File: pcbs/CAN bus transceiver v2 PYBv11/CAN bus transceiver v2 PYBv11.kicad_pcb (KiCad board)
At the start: 2 copper layers, 5 parts, among them P1 CONN_01X16, P2 CONN_01X02, P3 CONN_01X16, U1 TCAN337GDR, U2 TCAN337GDR

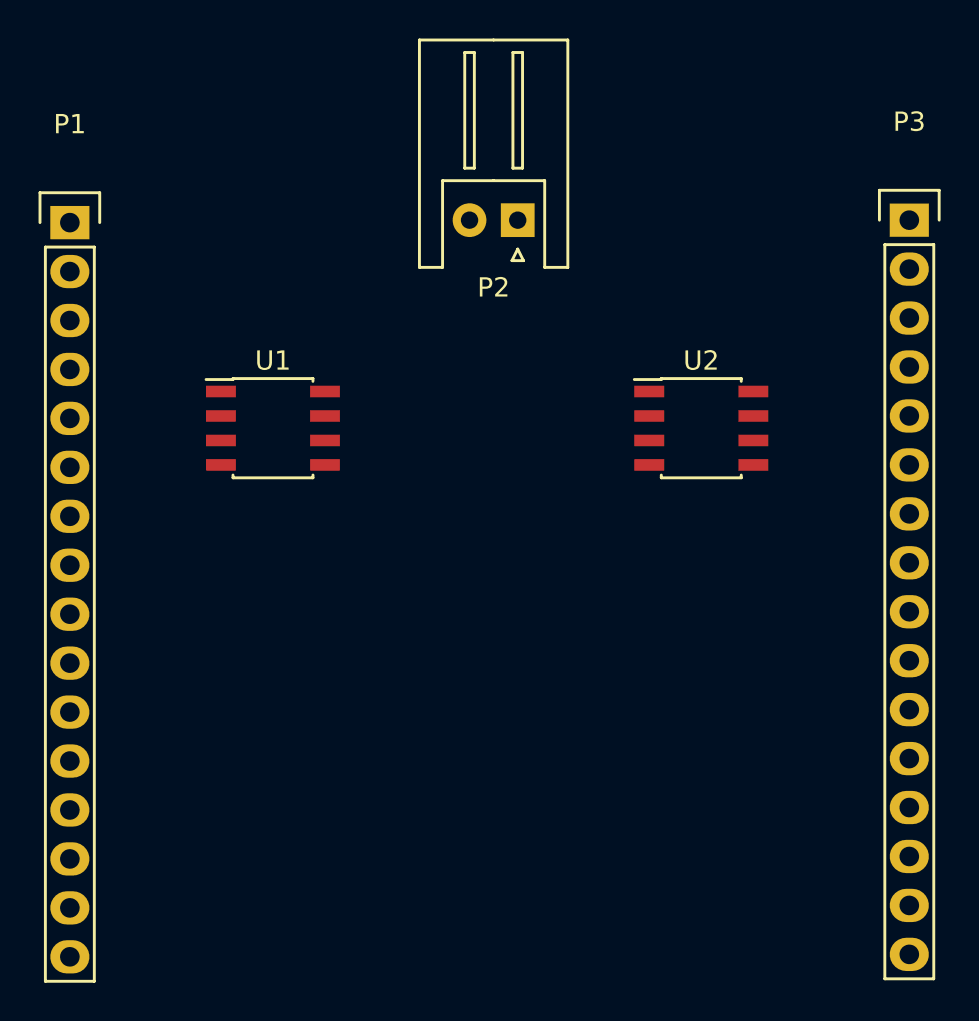
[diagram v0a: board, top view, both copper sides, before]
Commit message: working on CAN bus transceiver v2 PYBv11 shield
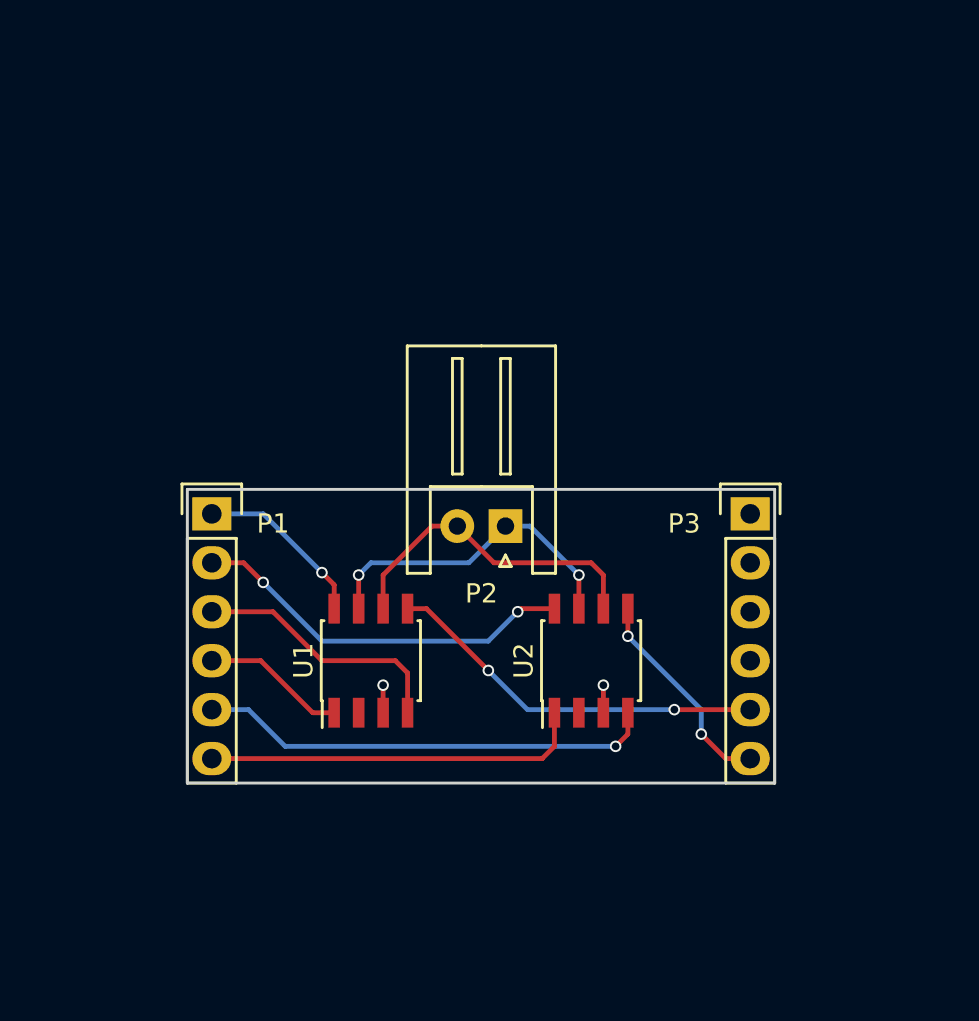
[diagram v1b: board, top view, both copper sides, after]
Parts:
- P1, P3: value CONN_01X16 -> CONN_01X06; footprint Pin_Headers:Pin_Header_Straight_1x16 -> Pin_Headers:Pin_Header_Straight_1x06
- moved P3 17.3 mm to (111.1, 91.4)
- moved P1 16.8 mm to (83.2, 91.4)
- moved P2 15.9 mm to (98.4, 92.1)
- moved U2 13.4 mm to (102.9, 99.1), turned to 90 degrees
- moved U1 13.1 mm to (91.4, 99.1), turned to 90 degrees
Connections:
- P3 pad 1: Net-(P3-Pad1) -> (no net)
- P3 pad 4: Net-(P3-Pad4) -> (no net)
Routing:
- net Net-(P1-Pad5): track 0.00 -> 23.8 mm, vias 0 -> 1
- net Net-(P1-Pad2): track 0.00 -> 20.2 mm, vias 0 -> 2
- net Net-(P3-Pad5): track 0.00 -> 20.0 mm, vias 0 -> 2
- net Net-(P1-Pad6): track 0.00 -> 19.8 mm
- net Net-(P2-Pad2): track 0.00 -> 17.0 mm
- net Net-(P2-Pad1): track 0.00 -> 17.0 mm, vias 0 -> 2
- net Net-(P1-Pad3): track 0.00 -> 13.5 mm
- net Net-(P3-Pad6): track 0.00 -> 11.2 mm, vias 0 -> 2
- net Net-(P1-Pad1): track 0.00 -> 9.11 mm, vias 0 -> 1
- net Net-(P1-Pad4): track 0.00 -> 7.47 mm
- net +3V3: track 0.00 -> 2.86 mm, vias 0 -> 2
- added copper zone on B.Cu, net +3V3
- added copper zone on F.Cu, net GND
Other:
- board outline added: 30.5 x 15.2 mm
- board text added: "3V3"
- board text added: "GND"
- board text added: "Y1"
- board text added: "Y11"
- board text added: "Y12"
- board text added: "Y2"
- board text added: "Y3"
- board text added: "Y4"
- board text added: "Y5"
- board text added: "Y6"

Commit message: working on CAN bus transceiver v2 PYBv11 shield
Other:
- board text added: "CAN bus transceiver shield v2 for PyBoard v 1.1"
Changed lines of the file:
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@@
     (links 16)
     (no_connects 0)
-    (area 81.839999 90.094999 112.470001 105.485001)
+    (area 63.270001 74.77 116.158334 117.000001)
     (thickness 1.6)
-    (drawings 18)
+    (drawings 19)
     (tracks 65)
     (zones 0)
@@
     (visible_elements FFFFFF7F)
     (pcbplotparams
-      (layerselection 0x00030_80000001)
-      (usegerberextensions false)
+      (layerselection 0x010f0_80000001)
+      (usegerberextensions true)
+      (gerberprecision 5)
       (excludeedgelayer true)
       (linewidth 0.100000)
@@
       (outputformat 1)
       (mirror false)
-      (drillshape 1)
+      (drillshape 0)
       (scaleselection 1)
-      (outputdirectory ""))
+      (outputdirectory plots/))
   )
   (net 0 "")
@@
     )
   )
+  (gr_text "CAN bus transceiver shield v2 for PyBoard v 1.1" (at 97.028 104.648) (layer B.SilkS)
+    (effects (font (size 0.5 0.5) (thickness 0.1)) (justify mirror))
+  )
   (gr_text 3V3 (at 108.712 93.98) (layer B.SilkS)

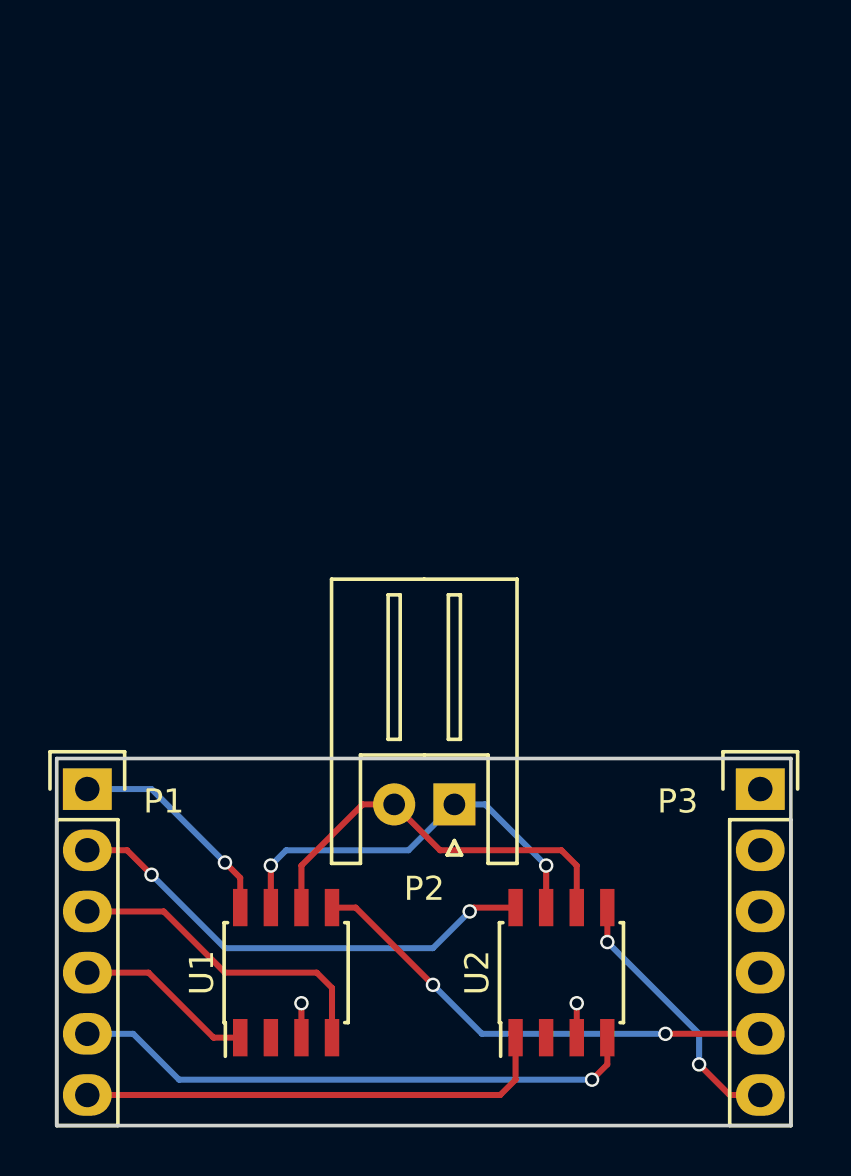
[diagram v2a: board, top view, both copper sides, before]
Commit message: working on CAN bus transceiver v2 PYBv11 shield
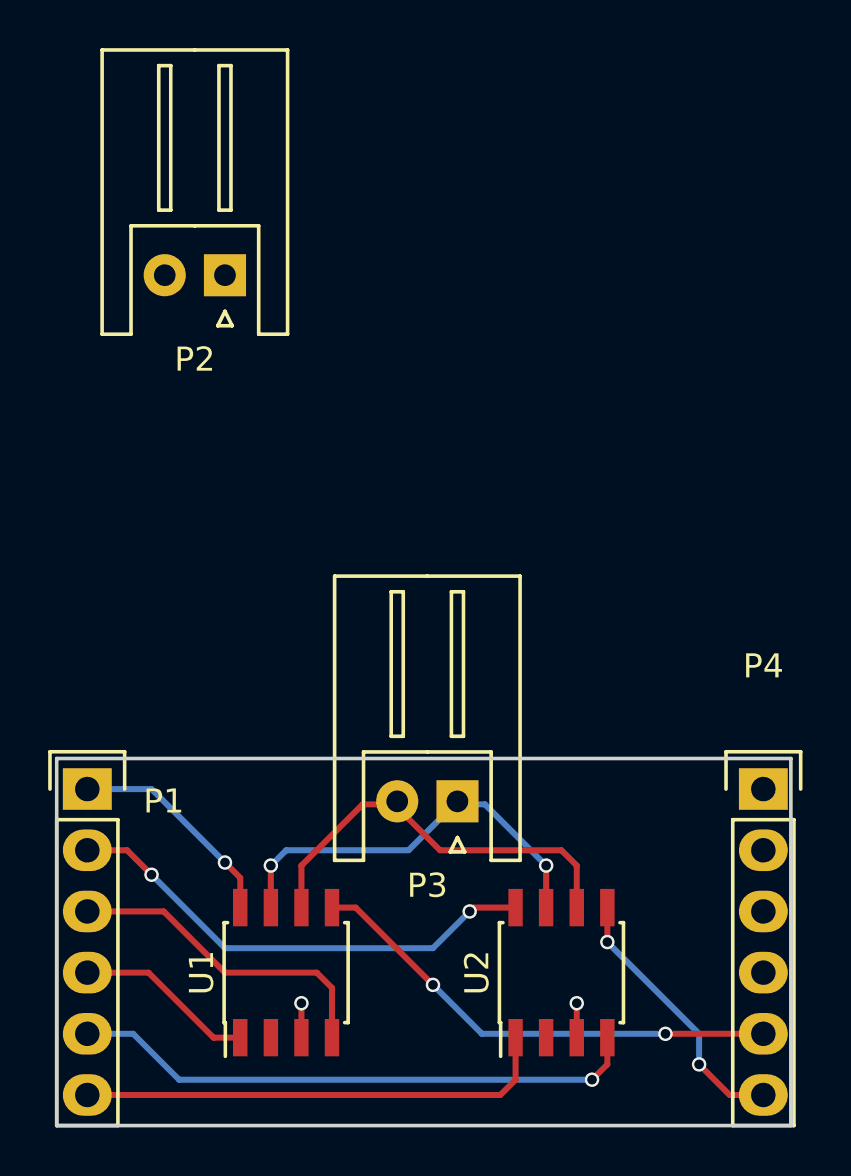
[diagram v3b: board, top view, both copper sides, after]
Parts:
- added P4: CONN_01X06, Pin_Headers:Pin_Header_Straight_1x06, F.Cu at (111.3, 91.4)
- P3: value CONN_01X06 -> CONN_01X02; footprint Pin_Headers:Pin_Header_Straight_1x06 -> Connectors_JST:JST_XH_S02B-XH-A_02x2.50mm_Angled
- moved P2 23.9 mm to (88.9, 70.1)
- moved P3 12.6 mm to (98.6, 91.9), turned to 180 degrees
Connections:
- P2 pad 1: Net-(P2-Pad1) -> (no net)
- P2 pad 2: Net-(P2-Pad2) -> (no net)
- P3 pad 1: (no net) -> Net-(P3-Pad1)
- P3 pad 2: +3V3 -> Net-(P3-Pad2)
- U1 pad 5: Net-(P3-Pad5) -> Net-(P4-Pad5)
- U1 pad 6: Net-(P2-Pad2) -> Net-(P3-Pad2)
- U1 pad 7: Net-(P2-Pad1) -> Net-(P3-Pad1)
- U2 pad 5: Net-(P3-Pad6) -> Net-(P4-Pad6)
- U2 pad 6: Net-(P2-Pad2) -> Net-(P3-Pad2)
- U2 pad 7: Net-(P2-Pad1) -> Net-(P3-Pad1)
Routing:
- net Net-(P4-Pad5): track 0.00 -> 20.0 mm, vias 0 -> 2
- net Net-(P3-Pad5): track 20.0 -> 0.00 mm, vias 2 -> 0
- net Net-(P3-Pad2): track 0.00 -> 17.0 mm
- net Net-(P2-Pad2): track 17.0 -> 0.00 mm
- net Net-(P3-Pad1): track 0.00 -> 17.0 mm, vias 0 -> 2
- net Net-(P2-Pad1): track 17.0 -> 0.00 mm, vias 2 -> 0
- net Net-(P4-Pad6): track 0.00 -> 11.2 mm, vias 0 -> 2
- net Net-(P3-Pad6): track 11.2 -> 0.00 mm, vias 2 -> 0

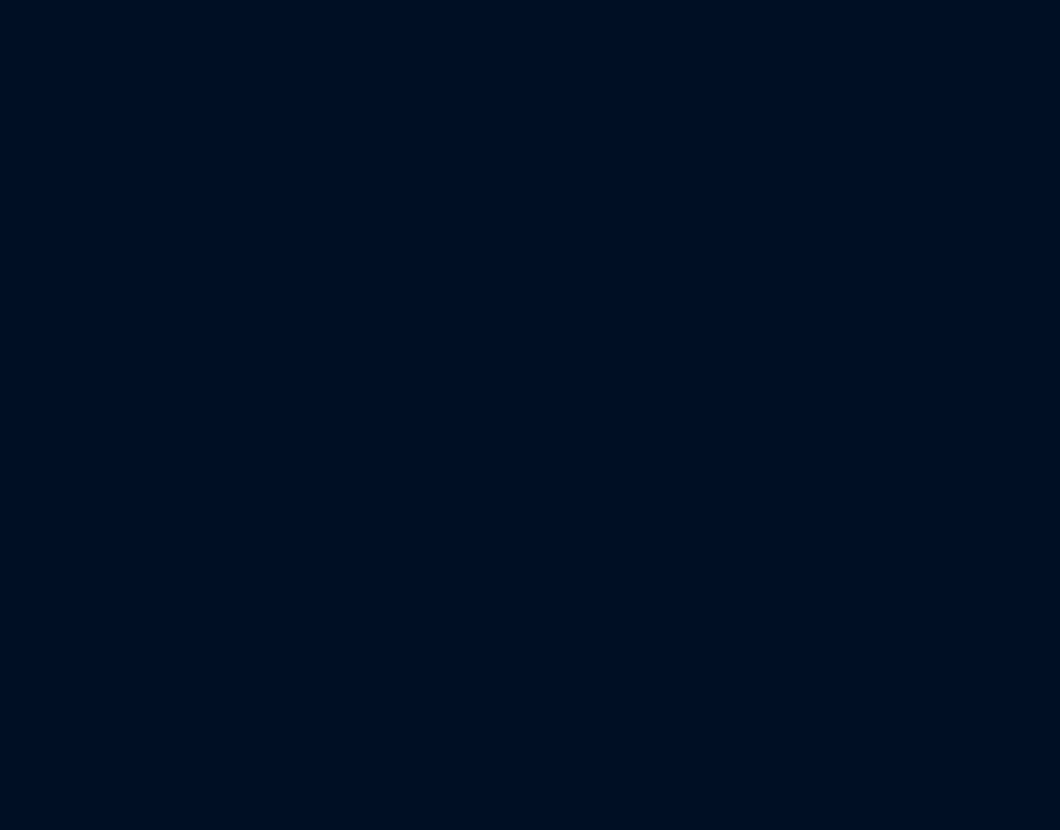
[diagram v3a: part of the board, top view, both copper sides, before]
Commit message: working on CAN bus transceiver v2 PYBv11 shield
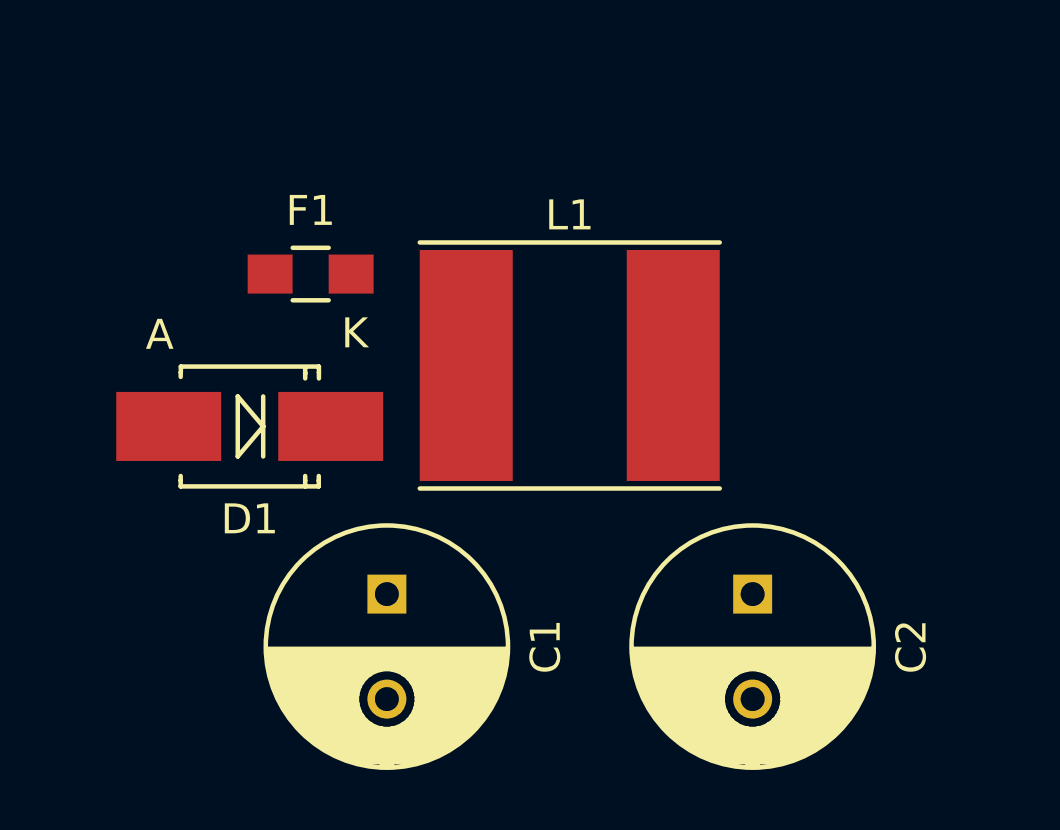
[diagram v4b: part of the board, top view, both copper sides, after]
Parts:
- added C1: CP1, Capacitors_ThroughHole:C_Radial_D8_L11.5_P3.5, F.Cu at (92.5, 135.6)
- added C2: CP1, Capacitors_ThroughHole:C_Radial_D8_L11.5_P3.5, F.Cu at (104.6, 135.6)
- added D1: ZENER, Diodes_SMD:SMB_Handsoldering, F.Cu at (87.9, 130.0)
- added F1: FUSE, Resistors_SMD:R_0805_HandSoldering, F.Cu at (89.9, 125.0)
- added L1: INDUCTOR, Inductors:Inductor_Taiyo-Yuden_NR-80xx_HandSoldering, F.Cu at (98.6, 128.0)

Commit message: doc: added docs for Pioneer AVH-X7500BT and Texas Instruments LM3489
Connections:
- C1 pad 2: Net-(C1-Pad2) -> GND
- C2 pad 2: Net-(C1-Pad2) -> GND
- D1 pad 2: Net-(C1-Pad2) -> GND
- F1 pad 1: (no net) -> +12V
- P2 pad 1: (no net) -> +12V
- P2 pad 2: (no net) -> GND
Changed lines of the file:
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@@
 (kicad_pcb (version 4) (host pcbnew 4.0.4-stable)
   (general
-    (links 22)
-    (no_connects 6)
+    (links 25)
+    (no_connects 9)
     (area 81.839999 90.094999 112.470001 105.485001)
     (thickness 1.6)
@@
   (net 11 "Net-(P4-Pad5)")
   (net 12 "Net-(P4-Pad6)")
-  (net 13 "Net-(C1-Pad2)")
-  (net 14 "Net-(C1-Pad1)")
-  (net 15 "Net-(C2-Pad1)")
+  (net 13 "Net-(C1-Pad1)")
+  (net 14 "Net-(C2-Pad1)")
+  (net 15 +12V)
   (net_class Default "This is the default net class."
     (clearance 0.2)
@@
     (uvia_dia 0.3)
     (uvia_drill 0.1)
+    (add_net +12V)
     (add_net +3V3)
     (add_net GND)
     (add_net "Net-(C1-Pad1)")
-    (add_net "Net-(C1-Pad2)")
     (add_net "Net-(C2-Pad1)")
     (add_net "Net-(P1-Pad1)")
@@
     (fp_line (start -0.3 -2.1) (end 0.3 -2.1) (layer F.SilkS) (width 0.15))
     (fp_line (start 0.3 -2.1) (end 0 -1.5) (layer F.SilkS) (width 0.15))
-    (pad 1 thru_hole rect (at 0 0 180) (size 1.75 1.75) (drill 0.9) (layers *.Cu *.Mask F.SilkS))
-    (pad 2 thru_hole circle (at 2.5 0 180) (size 1.75 1.75) (drill 0.9) (layers *.Cu *.Mask F.SilkS))
+    (pad 1 thru_hole rect (at 0 0 180) (size 1.75 1.75) (drill 0.9) (layers *.Cu *.Mask F.SilkS)
+      (net 15 +12V))
+    (pad 2 thru_hole circle (at 2.5 0 180) (size 1.75 1.75) (drill 0.9) (layers *.Cu *.Mask F.SilkS)
+      (net 7 GND))
     (model Connectors_JST.3dshapes/JST_XH_S02B-XH-A_02x2.50mm_Angled.wrl
       (at (xyz 0 0 0))
@@
     (fp_circle (center 1.75 0) (end 1.75 -4.3) (layer F.CrtYd) (width 0.05))
     (pad 2 thru_hole circle (at 3.5 0 270) (size 1.3 1.3) (drill 0.8) (layers *.Cu *.Mask F.SilkS)
-      (net 13 "Net-(C1-Pad2)"))
+      (net 7 GND))
     (pad 1 thru_hole rect (at 0 0 270) (size 1.3 1.3) (drill 0.8) (layers *.Cu *.Mask F.SilkS)
-      (net 14 "Net-(C1-Pad1)"))
+      (net 13 "Net-(C1-Pad1)"))
     (model Capacitors_ThroughHole.3dshapes/C_Radial_D8_L11.5_P3.5.wrl
       (at (xyz 0 0 0))
@@
     (fp_circle (center 1.75 0) (end 1.75 -4.3) (layer F.CrtYd) (width 0.05))
     (pad 2 thru_hole circle (at 3.5 0 270) (size 1.3 1.3) (drill 0.8) (layers *.Cu *.Mask F.SilkS)
-      (net 13 "Net-(C1-Pad2)"))
+      (net 7 GND))
     (pad 1 thru_hole rect (at 0 0 270) (size 1.3 1.3) (drill 0.8) (layers *.Cu *.Mask F.SilkS)
-      (net 15 "Net-(C2-Pad1)"))
+      (net 14 "Net-(C2-Pad1)"))
     (model Capacitors_ThroughHole.3dshapes/C_Radial_D8_L11.5_P3.5.wrl
       (at (xyz 0 0 0))
@@
     (fp_line (start 2.30124 -1.99898) (end 2.30124 -1.80086) (layer F.SilkS) (width 0.15))
     (pad 1 smd rect (at -2.70002 0 180) (size 3.50012 2.30124) (layers F.Cu F.Paste F.Mask)
-      (net 14 "Net-(C1-Pad1)"))
+      (net 13 "Net-(C1-Pad1)"))
     (pad 2 smd rect (at 2.70002 0 180) (size 3.50012 2.30124) (layers F.Cu F.Paste F.Mask)
-      (net 13 "Net-(C1-Pad2)"))
+      (net 7 GND))
     (model Diodes_SMD.3dshapes/SMB_Handsoldering.wrl
       (at (xyz 0 0 0))
@@
     (fp_line (start 0.6 0.875) (end -0.6 0.875) (layer F.SilkS) (width 0.15))
     (fp_line (start -0.6 -0.875) (end 0.6 -0.875) (layer F.SilkS) (width 0.15))
-    (pad 1 smd rect (at -1.35 0) (size 1.5 1.3) (layers F.Cu F.Paste F.Mask))
+    (pad 1 smd rect (at -1.35 0) (size 1.5 1.3) (layers F.Cu F.Paste F.Mask)
+      (net 15 +12V))
     (pad 2 smd rect (at 1.35 0) (size 1.5 1.3) (layers F.Cu F.Paste F.Mask)
-      (net 14 "Net-(C1-Pad1)"))
+      (net 13 "Net-(C1-Pad1)"))
     (model Resistors_SMD.3dshapes/R_0805_HandSoldering.wrl
       (at (xyz 0 0 0))
@@
     (fp_line (start 5.25 -4.25) (end -5.25 -4.25) (layer F.CrtYd) (width 0.05))
     (pad 1 smd rect (at -3.45 0) (size 3.1 7.7) (layers F.Cu F.Paste F.Mask)
-      (net 14 "Net-(C1-Pad1)"))
+      (net 13 "Net-(C1-Pad1)"))
     (pad 2 smd rect (at 3.45 0) (size 3.1 7.7) (layers F.Cu F.Paste F.Mask)
-      (net 15 "Net-(C2-Pad1)"))
+      (net 14 "Net-(C2-Pad1)"))
     (model Inductors.3dshapes/Inductor_Taiyo-Yuden_NR-80xx.wrl
       (at (xyz 0 0 0))
